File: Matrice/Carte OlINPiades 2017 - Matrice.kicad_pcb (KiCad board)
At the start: 2 copper layers, 200 x 200 mm, 1031 parts, among them P1 CONN_01X32, P2 CONN_01X32

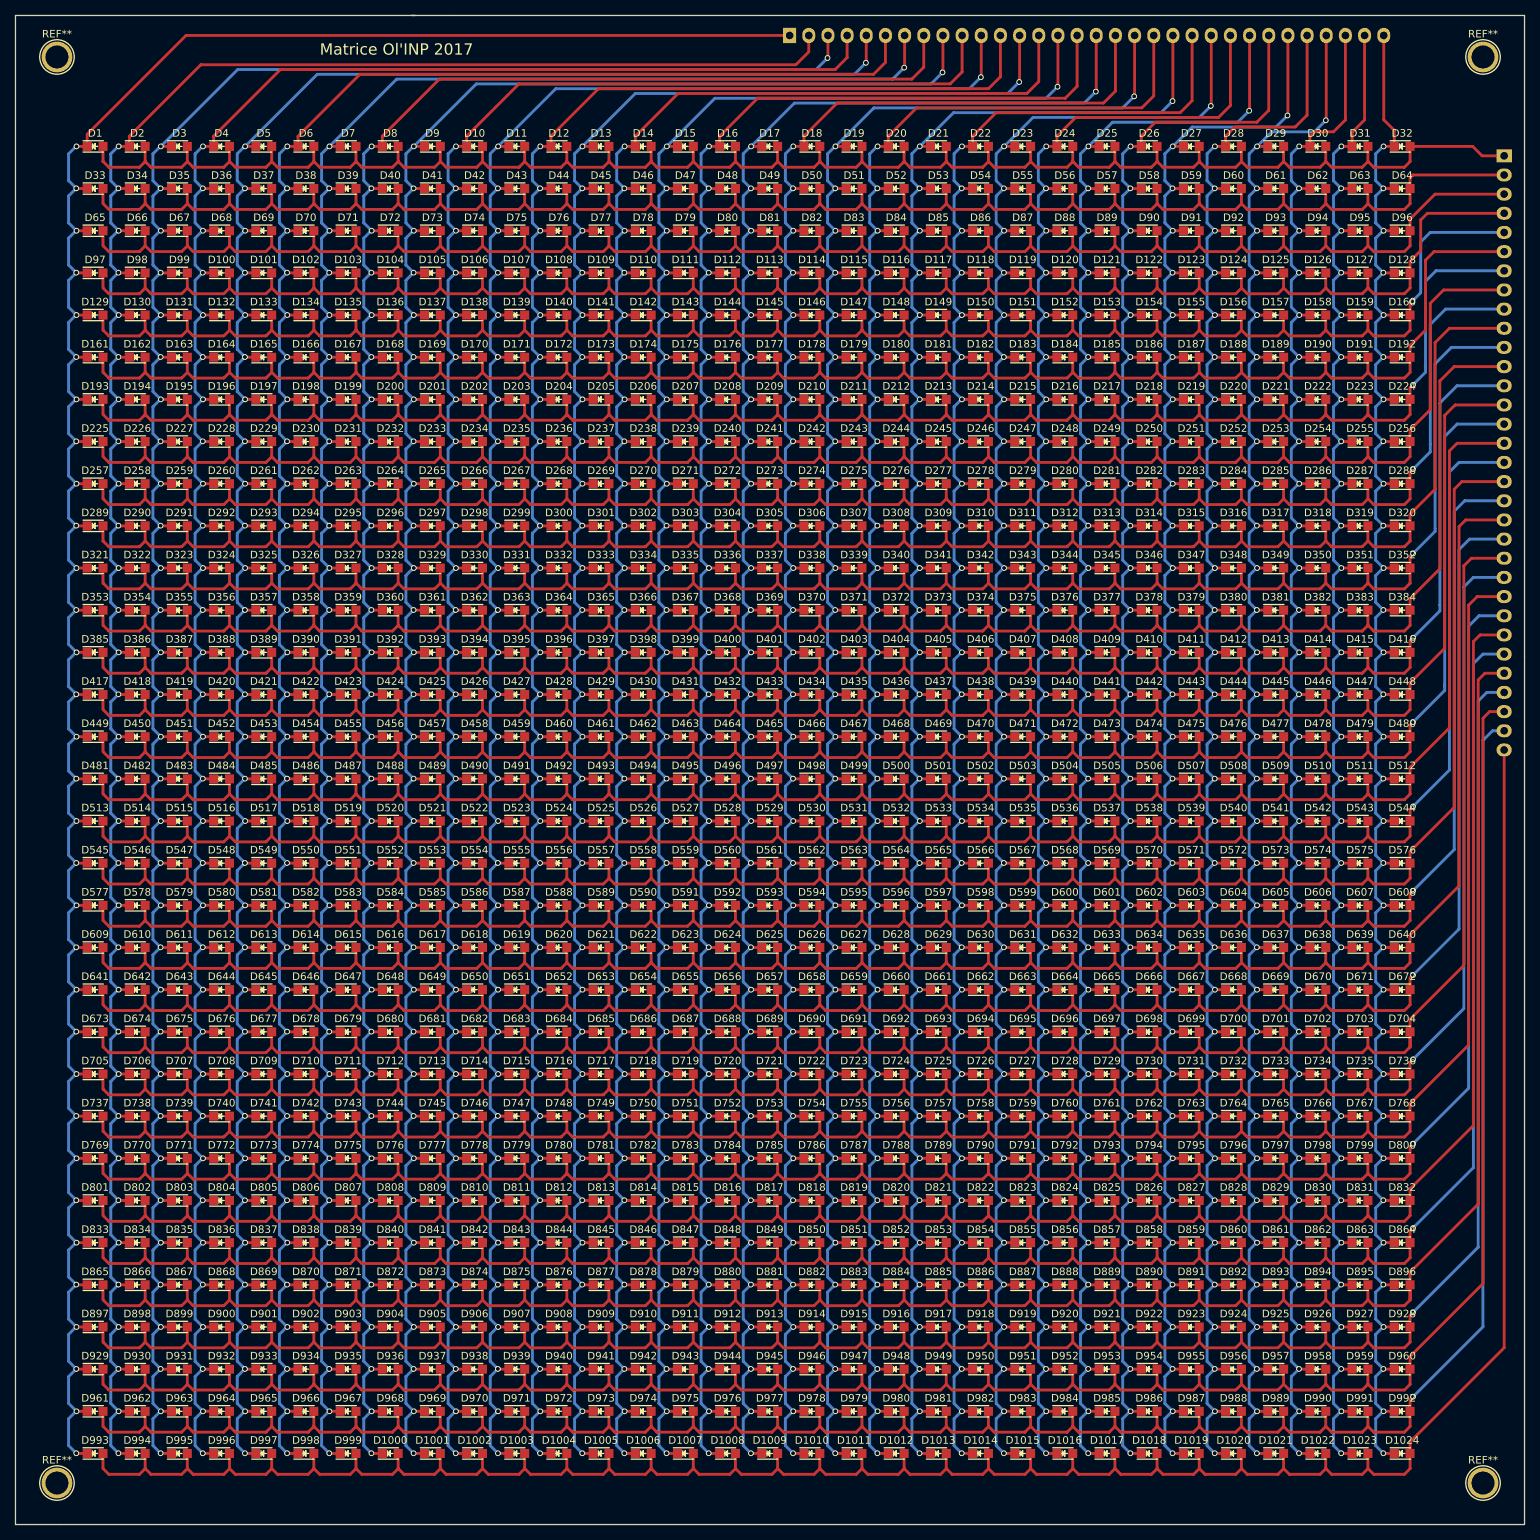
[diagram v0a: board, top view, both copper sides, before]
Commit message: Port matrice to kicad 5
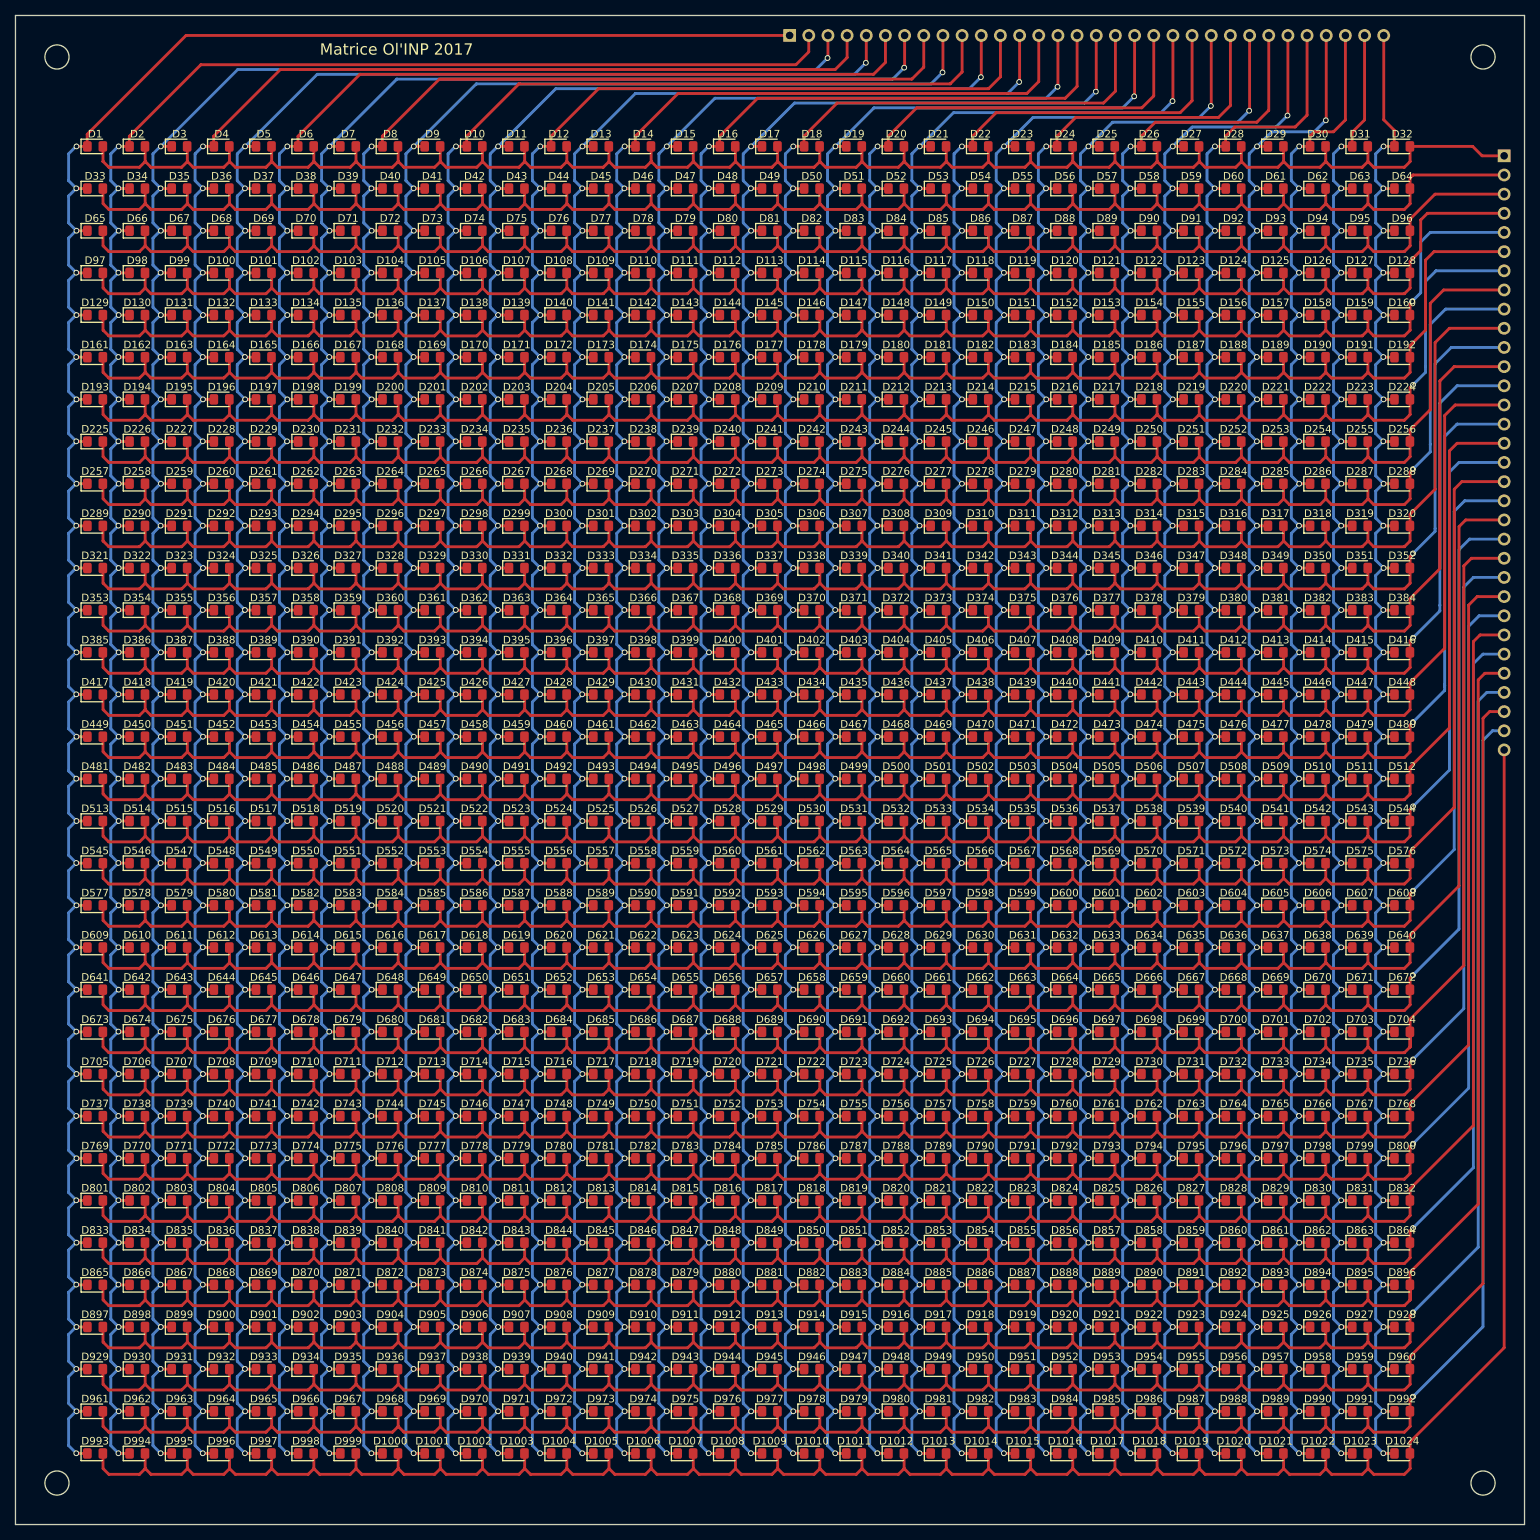
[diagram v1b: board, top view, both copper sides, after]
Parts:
- D1, D10, D100, D1000, D1001, D1002, D1003, D1004, D1005, D1006, D1007, D1008, D1009, D101, D1010, D1011, D1012, D1013, D1014, D1015, D1016, D1017, D1018, D1019, D102, D1020, D1021, D1022, D1023, D1024, D103, D104, D105, D106, D107, D108, D109, D11, D110, D111, D112, D113, D114, D115, D116, D117, D118, D119, D12, D120, D121, D122, D123, D124, D125, D126, D127, D128, D129, D13, D130, D131, D132, D133, D134, D135, D136, D137, D138, D139, D14, D140, D141, D142, D143, D144, D145, D146, D147, D148, D149, D15, D150, D151, D152, D153, D154, D155, D156, D157, D158, D159, D16, D160, D161, D162, D163, D164, D165, D166, D167, D168, D169, D17, D170, D171, D172, D173, D174, D175, D176, D177, D178, D179, D18, D180, D181, D182, D183, D184, D185, D186, D187, D188, D189, D19, D190, D191, D192, D193, D194, D195, D196, D197, D198, D199, D2, D20, D200, D201, D202, D203, D204, D205, D206, D207, D208, D209, D21, D210, D211, D212, D213, D214, D215, D216, D217, D218, D219, D22, D220, D221, D222, D223, D224, D225, D226, D227, D228, D229, D23, D230, D231, D232, D233, D234, D235, D236, D237, D238, D239, D24, D240, D241, D242, D243, D244, D245, D246, D247, D248, D249, D25, D250, D251, D252, D253, D254, D255, D256, D257, D258, D259, D26, D260, D261, D262, D263, D264, D265, D266, D267, D268, D269, D27, D270, D271, D272, D273, D274, D275, D276, D277, D278, D279, D28, D280, D281, D282, D283, D284, D285, D286, D287, D288, D289, D29, D290, D291, D292, D293, D294, D295, D296, D297, D298, D299, D3, D30, D300, D301, D302, D303, D304, D305, D306, D307, D308, D309, D31, D310, D311, D312, D313, D314, D315, D316, D317, D318, D319, D32, D320, D321, D322, D323, D324, D325, D326, D327, D328, D329, D33, D330, D331, D332, D333, D334, D335, D336, D337, D338, D339, D34, D340, D341, D342, D343, D344, D345, D346, D347, D348, D349, D35, D350, D351, D352, D353, D354, D355, D356, D357, D358, D359, D36, D360, D361, D362, D363, D364, D365, D366, D367, D368, D369, D37, D370, D371, D372, D373, D374, D375, D376, D377, D378, D379, D38, D380, D381, D382, D383, D384, D385, D386, D387, D388, D389, D39, D390, D391, D392, D393, D394, D395, D396, D397, D398, D399, D4, D40, D400, D401, D402, D403, D404, D405, D406, D407, D408, D409, D41, D410, D411, D412, D413, D414, D415, D416, D417, D418, D419, D42, D420, D421, D422, D423, D424, D425, D426, D427, D428, D429, D43, D430, D431, D432, D433, D434, D435, D436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: footprint LEDs:LED_0805 -> LED_SMD:LED_0805_2012Metric_Pad1.15x1.40mm_HandSolder
- LOGO1: renamed from G***; value LOGO -> Logo_Open_Hardware_Small; footprint drawings:robotronik_logo_big -> Matrice:robotronik_logo_big
- P1, P2: footprint Pin_Headers:Pin_Header_Straight_1x32 -> Connector_PinHeader_2.54mm:PinHeader_1x32_P2.54mm_Vertical
- PAD1, PAD2, PAD3, PAD4: renamed from REF**; value 1pin -> MountingHole; footprint Connect:1pin -> MountingHole:MountingHole_3.2mm_M3
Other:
- outline, holes or cut-outs redrawn
